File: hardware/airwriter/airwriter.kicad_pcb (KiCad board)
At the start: 2 copper layers, 52 x 78 mm, 60 parts, among them J1 USB-C 5V in, J2 Mini-DIN-8 to printer, J3 Bring-up USB/UART, J4 Mini-DIN-8 LocalTalk, J6 I2C / Qwiic, SW1 CONFIG/BOOT, SW2 MODE/TEST, U1 ESP32-S3-WROOM-1-N8R2, U2 MAX3490ESA+, U3 MAX3232ESE+, U4 AP7361C-33E, U5 USBLC6-2SC6, U6 SP3485EN-L, U7 PIC12F1840-I/P, U8 SP3485EN-L

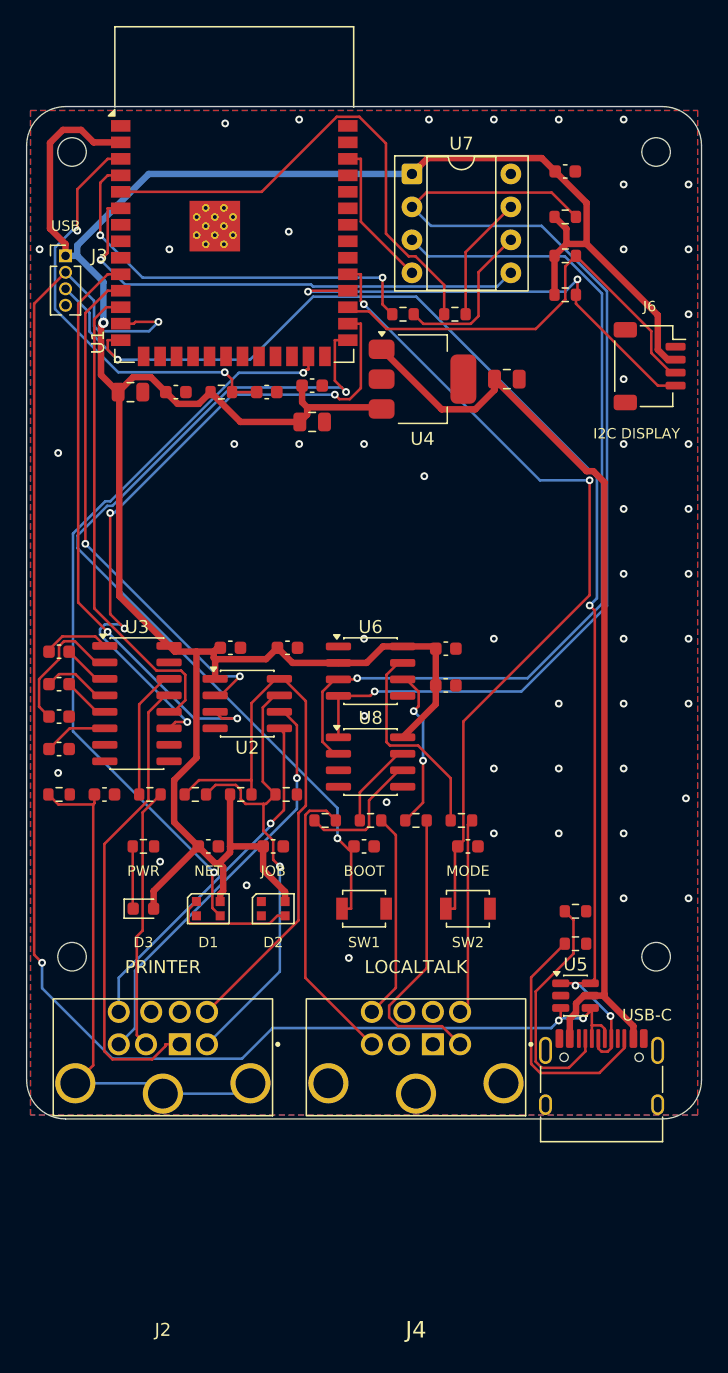
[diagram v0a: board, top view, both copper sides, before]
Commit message: Point the indicators at the viewer and make BOOT two pads
Components sit on the face that becomes the underside, so every indicator was firing
away from the person looking at the board. All three are reverse-mount now, emitting
toward the board -- and instead of the hole their footprints expect, they shine into
a bare-FR4 window, which is the logo recipe at small scale.

  D1, D2   WS2812B-2020  ->  SK6812MINI-E   LCSC C5149201, $0.045
  D3       0603 green    ->  LED_1206 ReverseMount
  SW1      B3U-1000P     ->  two bare pads, SolderJumper-2_P1.3mm_Open

The pin numbering changed and the wiring did not. WS2812B-2020 numbers its pins
DOUT-VSS-DIN-VDD; SK6812 numbers them VSS-DIN-VDD-DOUT. But both KiCad symbols put
the same functions at the same coordinates, so swapping lib_id moved every net
correctly and not one label had to move. Checked against the exported netlist.
Firmware is untouched -- SK6812 is the same one-wire protocol at the same 800kbit/s.

BOOT stops being a switch. With the USB-C carrying data, esptool drives the S3 into
download mode over the wire, so the two pads are just insurance you bridge with
tweezers. It also removes the last part that would have wanted a hole in the visible
face. MODE stays a real switch and still faces into the housing; that one is open.

The strip re-spaced -- the SK6812MINI-E is 7.3mm wide against the WS2812B's 3.0 -- and
now runs x 108.9 to 136.3, between mounting hole H3 and the power column.

New trap, documented: D1, D2 and D3 report lib_footprint_mismatch on purpose. Their
library footprints carry a cutout (Edge.Cuts on the SK6812, an NPTH slot on the 1206)
because they are drawn to shine through a hole. Re-importing any of them will punch
the holes back in, same as U1's 0.30mm vias.

DRC is 4 violations and all four are that mismatch. Drill floor 0.300mm, fab
regenerated, ERC unchanged bar the two expected flattened-symbol warnings.
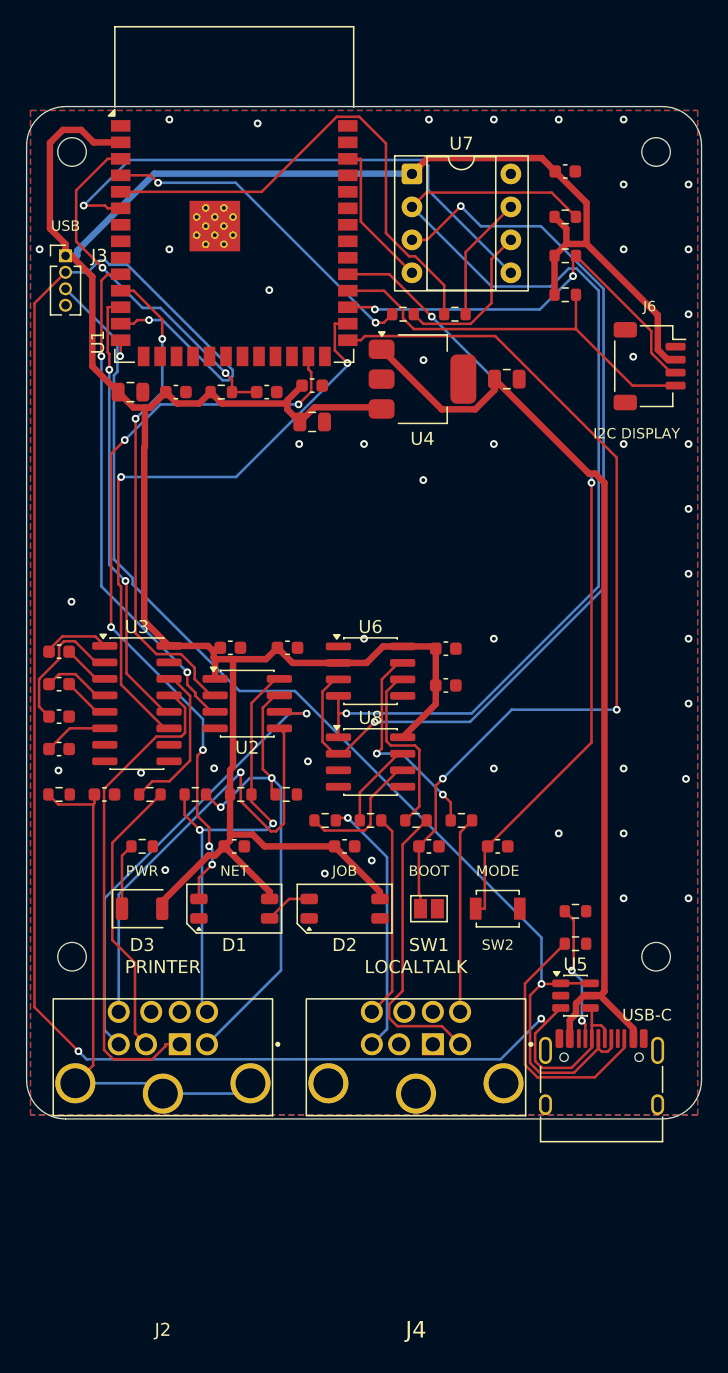
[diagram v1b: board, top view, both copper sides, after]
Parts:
- D1, D2: footprint LED_SMD:LED_WS2812B-2020_PLCC4_2.0x2.0mm -> LED_SMD:LED_SK6812MINI-E_3.2x2.8mm_P1.5mm_ReverseMount
- D3: footprint LED_SMD:LED_0603_1608Metric -> LED_SMD:LED_1206_3216Metric_ReverseMount_Hole1.8x2.4mm
- SW1: footprint Button_Switch_SMD:SW_SPST_B3U-1000P -> Jumper:SolderJumper-2_P1.3mm_Open_Pad1.0x1.5mm
- moved C20 5.50 mm to (124.5, 117.0)
- moved D2 5.50 mm to (124.5, 121.8)
- moved C7 5.00 mm to (131.0, 117.0)
- moved SW1 5.00 mm to (131.0, 121.8)
- moved C19 2.30 mm to (136.3, 117.0)
- moved SW2 2.30 mm to (136.3, 121.8)
- moved C8 2.00 mm to (116.0, 117.0)
- moved D1 2.00 mm to (116.0, 121.8)
- moved D3 0.10 mm to (108.9, 121.8)
- moved R17 0.10 mm to (108.9, 117.0)
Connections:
- D1 pad 1: /LED_CHAIN -> /GND
- D1 pad 2: /GND -> /LED_DATA
- D1 pad 3: /LED_DATA -> /+3V3
- D1 pad 4: /+3V3 -> /LED_CHAIN
- D2 pad 1: (no net) -> /GND
- D2 pad 2: /GND -> /LED_CHAIN
- D2 pad 3: /LED_CHAIN -> /+3V3
- D2 pad 4: /+3V3 -> (no net)
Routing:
- net /USB_DM: track 121.4 -> 143.2 mm, vias 4 -> 3
- net /USB_DP: track 104.8 -> 92.2 mm, vias 4 -> 2
- net /PR_RXD_P: track 27.3 -> 36.6 mm
- net /PR_TXD_P: track 45.4 -> 36.1 mm, vias 0 -> 2
- net /CC1: track 18.6 -> 10.6 mm, vias 0 -> 2
- net /UART_TX: track 45.1 -> 38.7 mm
- net /LT_UART_TX: track 32.1 -> 25.9 mm
- net /LED_CHAIN: track 9.55 -> 3.67 mm
- net /HSKI_DRV: track 52.7 -> 46.9 mm, vias 4 -> 2
- net /EN: track 33.2 -> 27.7 mm
- net /I2C_SCL: track 36.5 -> 31.3 mm, vias 2 -> 0
- net /LT_DE: track 70.1 -> 74.4 mm, vias 1 -> 2
- net /LT_CTS: track 38.1 -> 42.0 mm
- net /PR_RXD_N: track 32.0 -> 35.3 mm
- net /UART_CTS: track 37.4 -> 34.3 mm, vias 0 -> 2
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
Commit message: Light the logo with a cavity bounce off three more pixels
Reverse-mount LEDs make a local pool where they sit and do not spread sideways, so
sitting four of them behind a 33mm wordmark would have given four bright patches and
dim gaps between. D4, D5 and D6 are top-firing SK6812MINI instead, shining down into
the printed housing; a white cavity floor bounces the light back up through the
window already diffused, which is what a wide even glow wants.

They sit outside the logo keepout -- (105.5, 93), (146.5, 93), (115, 86.3) -- because
anything under the window would block light coming back up. For a light box the
position barely matters; the cavity floods.

All six pixels are one chain on one wire. U1 IO48 to D1, D1 to D2, then D2's DOUT,
which was hanging unconnected, carries on through D4, D5, D6 over LOGO_CH1/2/3. No
new GPIO, and the logo becomes addressable -- any colour, any animation, same
protocol. Firmware changes one constant from 2 pixels to 6.

SK6812 rather than WS2812B for a real reason found on the way: WS2812B wants 3.5V
minimum and this rail is 3.3V, so the original D1 and D2 were out of spec and nobody
had noticed. Every SK6812 on the board is specified down to 3.3V.

Netlist verified pixel by pixel. ERC is nine lib_symbol_mismatch warnings, all from
symbols flattened into the schematic rather than carried by (extends). DRC is four
violations, all the deliberate cutout removals plus U1. Drill floor 0.300mm.
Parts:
- added D4: SK6812MINI, LED_SMD:LED_SK6812MINI_PLCC4_3.5x3.5mm_P1.75mm, F.Cu at (105.5, 93.0)
- added D5: SK6812MINI, LED_SMD:LED_SK6812MINI_PLCC4_3.5x3.5mm_P1.75mm, F.Cu at (146.5, 93.0)
- added D6: SK6812MINI, LED_SMD:LED_SK6812MINI_PLCC4_3.5x3.5mm_P1.75mm, F.Cu at (115.0, 86.3)
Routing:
- net /HSKI_DRV: track 46.9 -> 0.00 mm, vias 2 -> 0
- net /USB_DM: track 143.2 -> 96.5 mm, vias 3 -> 4
- net /BTN_MODE: track 62.6 -> 99.1 mm
- net /+3V3: track 215.3 -> 243.1 mm
- net /LT_DE: track 74.4 -> 62.7 mm
- net /PR_RXD_P: track 36.6 -> 27.2 mm
- net /CC1: track 10.6 -> 18.6 mm, vias 2 -> 0
- net /PR_TXD_P: track 36.1 -> 42.9 mm
- net /LT_DATA: track 82.2 -> 75.4 mm, vias 1 -> 2
- net /BOOT_CFG: track 70.6 -> 64.8 mm
- net /USB_DP: track 92.2 -> 86.5 mm, vias 2 -> 3
- net /UART_CTS: track 34.3 -> 39.4 mm
- net /PR_TXD_N: track 38.3 -> 43.2 mm
- net /UART_TX: track 38.7 -> 42.6 mm, vias 2 -> 4
- net /LT_UART_TX: track 25.9 -> 29.1 mm, vias 2 -> 0
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
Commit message: Make MODE a gold touch pad on the face you actually look at
SW2 stops being a switch. It is now airwriter:TouchPad_Comb_9x7mm -- a comb electrode
on B.Cu with a ground guard bar, mask opened over both so a bare finger meets ENIG
gold on the visible face. The comb is one net; the interleaving is visual. The S3
senses self-capacitance, where a continuous electrode beats an interdigitated one, so
the look costs nothing.

  MODE moves IO38 -> IO14, because the S3 only does touch on IO1-IO14
  R20, 1k, in series: exposed metal on a GPIO is an ESD path and the S3 is rated
    around 2kV while a person carries far more
  C19 goes DNP rather than away -- 100nF across a touch pin would swamp a sense
    capacitance measured in picofarads, and leaving the pads means one part reverts
    MODE to a mechanical switch if touch disappoints

The eurorack precedent is split and worth recording. Make Noise's Rene uses resistive
touch, skin completing a circuit, and is known for not reading on dry hands -- that is
the failure I kept warning about. Synthux's Simple Touch is capacitive via an MPR121
and has no such problem. An MPR121 is twelve channels; overkill for one button when
the S3 has the peripheral built in.

Also corrects an earlier note in the handoff: bare gold is right here. Soldermask is
25 microns and barely matters either way, but exposed ENIG is more sensitive, is what
the synth world does, and is the whole point of paying for the finish.

DRC is four violations, all the deliberate cutout removals plus U1. ERC is nine
lib_symbol_mismatch from flattened symbols. Drill floor 0.300mm, fab regenerated.
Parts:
- added R20: 1k, Resistor_SMD:R_0603_1608Metric, F.Cu at (103.0, 117.0)
- SW2: value MODE/TEST -> MODE touch; footprint Button_Switch_SMD:SW_SPST_B3U-1000P -> airwriter:TouchPad_Comb_9x7mm; moved to B.Cu
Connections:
- U1 pad 22: unconnected-(U1-IO14-Pad22) -> /TOUCH_SENSE
- U1 pad 31: /BTN_MODE -> (no net)
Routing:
- net /BTN_MODE: track 99.1 -> 40.4 mm
- net /TOUCH_SENSE: track 0.00 -> 50.7 mm, vias 0 -> 2
- net /USB_DM: track 96.5 -> 110.3 mm, vias 4 -> 2
- net /PR_TXD_P: track 42.9 -> 34.1 mm, vias 2 -> 1
- net /BOOT_CFG: track 64.8 -> 72.6 mm
- net /LT_DATA: track 75.4 -> 82.2 mm, vias 2 -> 1
- net /PR_TXD_N: track 43.2 -> 36.4 mm, vias 2 -> 1
- net /PR_RXD_P: track 27.2 -> 33.8 mm, vias 1 -> 2
- net /PR_RXD_N: track 34.5 -> 41.0 mm
- net /USB_DP: track 86.5 -> 92.9 mm
- net /LT_DE: track 62.7 -> 68.0 mm, vias 2 -> 3
- net /CC1: track 18.6 -> 13.5 mm, vias 0 -> 2
- net /PR_HSKO: track 36.3 -> 31.4 mm, vias 0 -> 1
- net /LT_UART_TX: track 29.1 -> 25.4 mm, vias 0 -> 2
- net /UART_TX: track 42.6 -> 39.9 mm, vias 4 -> 0
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
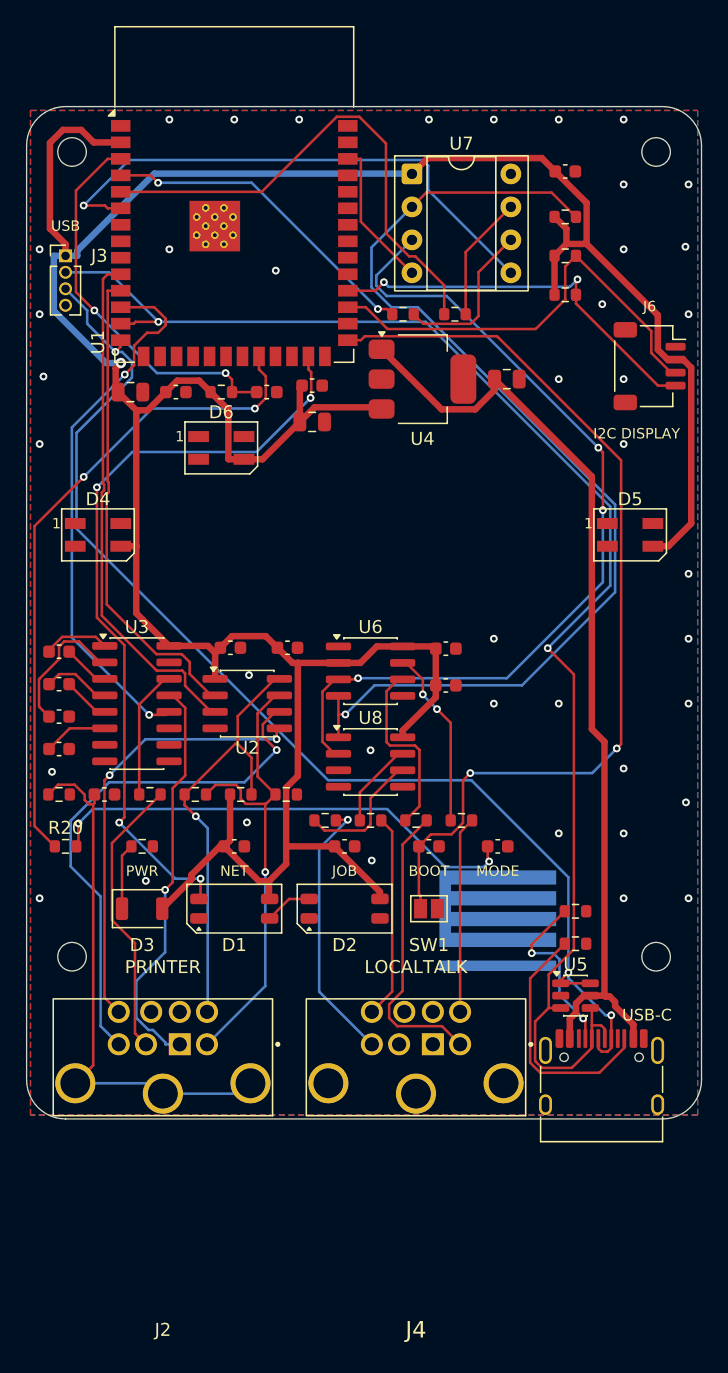
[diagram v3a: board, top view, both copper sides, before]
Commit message: Put the touch pattern in the soldermask instead of the copper
The comb was chunky and, worse, it cut the electrode up. Self-capacitance wants
unbroken area, so carving the copper into fingers or a halftone trades sensitivity
for looks.

So the copper does not carry the pattern at all. The electrode is a solid 9.2mm disc
and the mask opens along eleven thin arcs, 0.18mm wide on a 0.45mm pitch, rotating
and lengthening as the radius grows so it reads as a ripple rather than a bullseye.
What you see is fine gold arcs on matte black; what the chip sees is a full disc.
Same trick as the logo -- mask carries the artwork, copper carries the function.

First attempt packed the arcs on a 0.265mm pitch, which left 0.045mm mask dams. That
is under half PCBWay's 0.1mm floor and would have flooded into one solid blob. At
0.45mm pitch the dams are 0.27mm, comfortably clear.

The footprint is generated, not drawn -- TouchPad_Arcs_D9mm.kicad_mod comes out of a
short script, so the rhythm can be re-cut by changing three numbers.

DRC still four violations, all the deliberate cutout removals plus U1. Drill floor
0.300mm, 18 mask apertures on the back layer, fab regenerated.
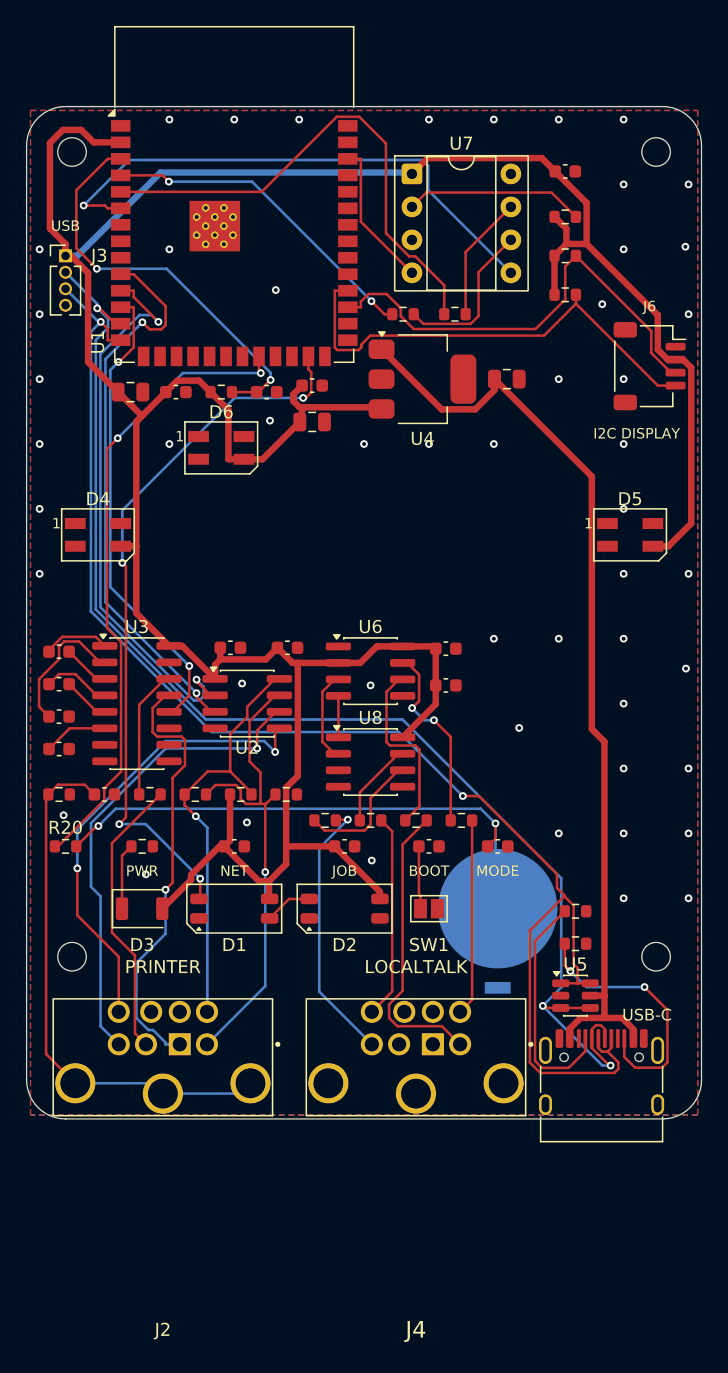
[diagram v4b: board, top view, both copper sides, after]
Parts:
- SW2: footprint airwriter:TouchPad_Comb_9x7mm -> airwriter:TouchPad_Arcs_D9mm
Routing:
- net /BOOT_CFG: track 72.6 -> 4.85 mm, vias 2 -> 0
- net /LT_DATA: track 82.2 -> 17.1 mm, vias 1 -> 0
- net /LT_DE: track 68.0 -> 7.10 mm, vias 3 -> 0
- net /USB_DP: track 92.9 -> 110.2 mm, vias 3 -> 2
- net /USB_DM: track 110.3 -> 101.2 mm, vias 2 -> 3
- net /UART_RX: track 37.1 -> 44.2 mm, vias 0 -> 2
- net /I2C_SCL: track 30.6 -> 36.6 mm, vias 2 -> 0
- net /UART_CTS: track 41.9 -> 36.3 mm
- net /CC1: track 13.5 -> 18.1 mm, vias 2 -> 0
- net /PR_RXD_N: track 41.0 -> 36.8 mm
- net /LED_DATA: track 59.2 -> 55.3 mm
- net /UART_TX: track 39.9 -> 43.0 mm, vias 0 -> 2
- net /BTN_MODE: track 40.4 -> 42.6 mm
- net /PR_HSKO: track 31.4 -> 33.5 mm
- net /PR_RXD_P: track 33.8 -> 35.7 mm
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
